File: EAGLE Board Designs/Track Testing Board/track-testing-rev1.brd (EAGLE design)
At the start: 100 x 80 mm, 20 parts, among them J1 CONNECTOR-4_μF_S_RA_, J2 CONNECTOR-4_μF_S_RA_, U1 VOLTAGE_REGULATOR_SOT-23-5_5V, U2 VOLTAGE_REFERENCE_SOIC-8_10V, U3 INA823DT, U4 INA823DT

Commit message: passes drc as is
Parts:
- moved RV1 0.51 mm to (49.8, 45.7)
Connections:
- net STRAIN_GAUGE1_AMPLIFIED: now also A1.D15; no longer A1.D14
- net STRAIN_GAUGE2_AMPLIFIED: now also A1.D14; no longer A1.D15
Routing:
- net STRAIN_GAUGE2_AMPLIFIED: track 46.8 -> 41.5 mm
- net STRAIN_GAUGE1_AMPLIFIED: track 42.9 -> 41.9 mm
- net OUT2-: track 7.01 -> 6.29 mm
- net OUT2+: track 25.8 -> 25.2 mm
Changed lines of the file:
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@@
 <attribute name="NAME" x="35.56" y="77.597" size="0.8128" layer="25" align="bottom-center"/>
 </element>
-<element name="RV1" library="HyTechDevices" package="0603-RES" value="10k" x="49.784" y="45.212" smashed="yes" rot="R180">
-<attribute name="10KOHM" value="https://www.digikey.com/en/products/detail/yageo/RT0603BRD0710KL/1072198" x="49.276" y="45.212" size="1.778" layer="27" rot="R180" display="off"/>
-<attribute name="NAME" x="49.784" y="44.577" size="0.8128" layer="25" font="vector" rot="R180" align="bottom-center"/>
+<element name="RV1" library="HyTechDevices" package="0603-RES" value="10k" x="49.784" y="45.72" smashed="yes" rot="R180">
+<attribute name="10KOHM" value="https://www.digikey.com/en/products/detail/yageo/RT0603BRD0710KL/1072198" x="49.276" y="45.72" size="1.778" layer="27" rot="R180" display="off"/>
+<attribute name="NAME" x="49.784" y="45.085" size="0.8128" layer="25" font="vector" rot="R180" align="bottom-center"/>
 </element>
 <element name="RV5" library="HyTechDevices" package="0603-RES" value="9.88k" x="48.26" y="47.752" smashed="yes">
@@
 <contactref element="U3" pad="4"/>
 <contactref element="J2" pad="2"/>
-<wire x1="30.936" y1="57.952" x2="30.988" y2="57.9" width="0.254" layer="1"/>
 <polygon width="0.254" layer="1">
 <vertex x="-0.508" y="80.772"/>
@@
 <contactref element="C5" pad="2"/>
 <wire x1="56.11" y1="62.2935" x2="56.11" y2="66.9163" width="0" layer="19" extent="1-1"/>
-<wire x1="58.9915" y1="53.467" x2="56.11" y2="62.2935" width="0" layer="19" extent="1-1"/>
+<wire x1="53.7845" y1="53.467" x2="56.11" y2="62.2935" width="0" layer="19" extent="1-1"/>
+<wire x1="58.9915" y1="53.467" x2="53.7845" y2="53.467" width="0" layer="19" extent="1-1"/>
 <wire x1="61.468" y1="54.114" x2="58.9915" y2="53.467" width="0" layer="19" extent="1-1"/>
-<wire x1="53.7845" y1="53.467" x2="58.9915" y2="53.467" width="0" layer="19" extent="1-1"/>
 <wire x1="48.934" y1="55.372" x2="53.7845" y2="53.467" width="0" layer="19" extent="1-1"/>
 <wire x1="43.18" y1="53.606" x2="48.934" y2="55.372" width="0" layer="19" extent="1-1"/>
 <wire x1="35.4965" y1="53.975" x2="43.18" y2="53.606" width="0" layer="19" extent="1-1"/>
 <wire x1="30.988" y1="57.9" x2="35.4965" y2="53.975" width="0" layer="19" extent="1-1"/>
-<wire x1="29.144" y1="57.444" x2="30.936" y2="57.952" width="0" layer="19" extent="1-1"/>
+<wire x1="29.144" y1="57.444" x2="30.988" y2="57.9" width="0" layer="19" extent="1-1"/>
 <wire x1="25.4" y1="55.384" x2="29.144" y2="57.444" width="0" layer="19" extent="1-1"/>
 <wire x1="61.468" y1="44.97" x2="58.9915" y2="53.467" width="0" layer="19" extent="1-1"/>
 <wire x1="58.9915" y1="44.323" x2="61.468" y2="44.97" width="0" layer="19" extent="1-1"/>
 <wire x1="53.7845" y1="44.323" x2="58.9915" y2="44.323" width="0" layer="19" extent="1-1"/>
-<wire x1="48.934" y1="45.212" x2="53.7845" y2="44.323" width="0" layer="19" extent="1-1"/>
+<wire x1="48.934" y1="45.72" x2="53.7845" y2="44.323" width="0" layer="19" extent="1-1"/>
 <wire x1="37.06" y1="66.9163" x2="30.988" y2="57.9" width="0" layer="19" extent="1-1"/>
 <wire x1="20.32" y1="39.37" x2="25.4" y2="55.384" width="0" layer="19" extent="1-1"/>
@@
 <wire x1="53.047" y1="45.593" x2="50.634" y2="43.18" width="0.254" layer="1"/>
 <wire x1="49.11" y1="43.18" x2="50.634" y2="43.18" width="0.254" layer="1"/>
-<wire x1="53.11" y1="62.2935" x2="53.61936875" y2="62.2935" width="0.254" layer="1"/>
 <wire x1="53.11" y1="62.2935" x2="54.356" y2="61.0475" width="0.254" layer="1"/>
 <wire x1="54.356" y1="61.0475" x2="54.356" y2="60.96" width="0.254" layer="1"/>
 <via x="54.356" y="60.96" extent="1-16" drill="0.35"/>
-<wire x1="54.356" y1="60.96" x2="54.864" y2="60.452" width="0.254" layer="16"/>
-<wire x1="54.864" y1="60.452" x2="54.864" y2="48.26" width="0.254" layer="16"/>
-<wire x1="55.88" y1="47.244" x2="55.88" y2="46.228" width="0.254" layer="16"/>
-<wire x1="55.88" y1="47.244" x2="54.864" y2="48.26" width="0.254" layer="16"/>
+<wire x1="54.356" y1="60.96" x2="55.88" y2="59.436" width="0.254" layer="16"/>
+<wire x1="55.88" y1="59.436" x2="55.88" y2="46.228" width="0.254" layer="16"/>
 <via x="55.88" y="46.228" extent="1-16" drill="0.35"/>
 <wire x1="55.88" y1="46.228" x2="55.245" y2="45.593" width="0.254" layer="1"/>
@@
 <contactref element="RV5" pad="2"/>
 <contactref element="U4" pad="2"/>
-<wire x1="50.634" y1="45.212" x2="52.285" y2="46.863" width="0.254" layer="1"/>
-<wire x1="52.285" y1="46.863" x2="53.7845" y2="46.863" width="0.254" layer="1"/>
+<wire x1="50.634" y1="45.72" x2="51.777" y2="46.863" width="0.254" layer="1"/>
+<wire x1="51.777" y1="46.863" x2="53.7845" y2="46.863" width="0.254" layer="1"/>
 <wire x1="49.11" y1="47.752" x2="50.634" y2="46.228" width="0.254" layer="1"/>
-<wire x1="50.634" y1="46.228" x2="50.634" y2="45.212" width="0.254" layer="1"/>
+<wire x1="50.634" y1="46.228" x2="50.634" y2="45.72" width="0.254" layer="1"/>
 </signal>
 <signal name="OUT1-">
@@
 <signal name="STRAIN_GAUGE1_AMPLIFIED">
 <contactref element="U3" pad="6"/>
-<contactref element="A1" pad="D14"/>
-<wire x1="20.32" y1="44.45" x2="26.67" y2="50.8" width="0.254" layer="1"/>
-<wire x1="26.67" y1="50.8" x2="54.356" y2="50.8" width="0.254" layer="1"/>
+<wire x1="47.498" y1="50.8" x2="54.356" y2="50.8" width="0.254" layer="1"/>
 <wire x1="54.356" y1="50.8" x2="58.293" y2="54.737" width="0.254" layer="1"/>
 <wire x1="58.293" y1="54.737" x2="58.9915" y2="54.737" width="0.254" layer="1"/>
+<contactref element="A1" pad="D15"/>
+<wire x1="20.32" y1="46.99" x2="43.688" y2="46.99" width="0.254" layer="1"/>
+<wire x1="43.688" y1="46.99" x2="47.498" y2="50.8" width="0.254" layer="1"/>
 </signal>
 <signal name="STRAIN_GAUGE2_AMPLIFIED">
 <contactref element="U4" pad="6"/>
-<contactref element="A1" pad="D15"/>
-<wire x1="20.32" y1="46.99" x2="18.796" y2="45.466" width="0.254" layer="1"/>
-<wire x1="18.796" y1="43.9932375" x2="19.6092375" y2="43.18" width="0.254" layer="1"/>
-<wire x1="59.1185" y1="45.72" x2="58.9915" y2="45.593" width="0.254" layer="1"/>
-<wire x1="18.796" y1="45.466" x2="18.796" y2="43.9932375" width="0.254" layer="1"/>
-<wire x1="44.704" y1="43.18" x2="46.228" y2="41.656" width="0.254" layer="1"/>
+<wire x1="43.434" y1="44.45" x2="46.228" y2="41.656" width="0.254" layer="1"/>
 <wire x1="46.228" y1="41.656" x2="53.848" y2="41.656" width="0.254" layer="1"/>
-<wire x1="58.8645" y1="45.72" x2="58.9915" y2="45.593" width="0.254" layer="1"/>
-<wire x1="19.6092375" y1="43.18" x2="44.704" y2="43.18" width="0.254" layer="1"/>
+<wire x1="20.32" y1="44.45" x2="43.434" y2="44.45" width="0.254" layer="1"/>
 <wire x1="57.785" y1="45.593" x2="58.9915" y2="45.593" width="0.254" layer="1"/>
 <wire x1="53.848" y1="41.656" x2="57.785" y2="45.593" width="0.254" layer="1"/>
+<contactref element="A1" pad="D14"/>
 </signal>
 <signal name="3.3V">

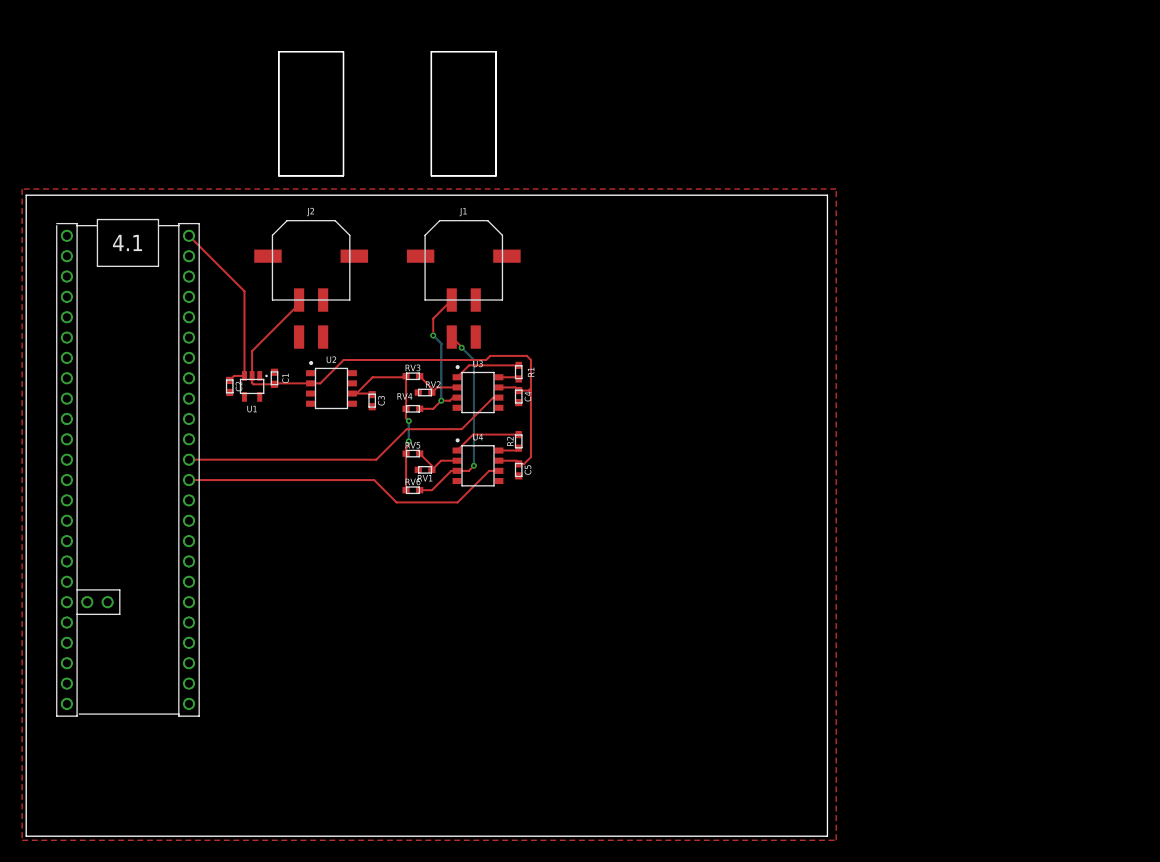
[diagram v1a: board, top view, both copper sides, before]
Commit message: 10 strain gauges and aero uart, passes drc
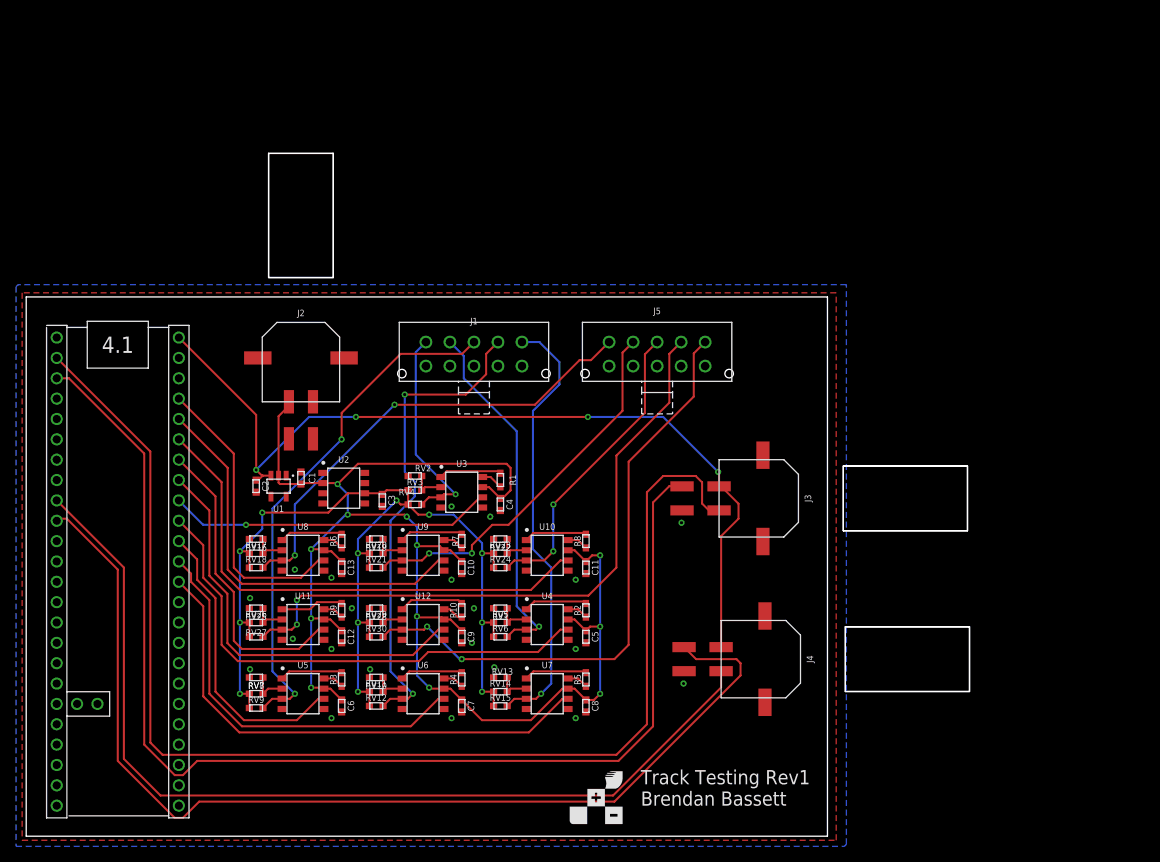
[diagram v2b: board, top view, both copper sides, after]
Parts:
- added C10, C11, C12, C13, C6, C7, C8, C9: CAPACITOR_0603_25V_0.1UF, HyTechDevices:0603-CAP
- added J3, J4: CONNECTOR-4_μF_S_RA_, HyTechDevices:MOLEX_MICROFIT_SMD_RIGHTANGLE_04_DUAL
- added J5: CONNECTOR-10_MF_T_V_, HyTechDevices:MOLEX_MICROFIT_PTH_VERTICAL_10_DUAL
- added R10, R3, R4, R5, R6, R7, R8, R9: RESISTOR_0603_1K, HyTechDevices:0603-RES
- added RV10, RV13, RV16, RV19, RV22, RV25, RV28, RV7: 10k, HyTechDevices:0603-RES
- added RV11, RV14, RV17, RV20, RV23, RV26, RV29, RV8: 9.88k, HyTechDevices:0603-RES
- added RV12, RV15, RV18, RV21, RV24, RV27, RV30, RV9: 118, HyTechDevices:0603-RES
- added U$15: (no value), HyTechManufacturing:LOGO_HYTECH_LARGE
- added U$16: (no value), HyTechManufacturing:LOGO_HYTECH_SQUARE_LARGE
- added U10, U11, U12, U5, U6, U7, U8, U9: INA823DT, HyTechDevices:SOIC-08(NARROW,0.15")
- J1: value CONNECTOR-4_μF_S_RA_ -> CONNECTOR-10_MF_T_V_; device HyTechDevices:MOLEX_MICROFIT_SMD_RIGHTANGLE_04_DUAL -> HyTechDevices:MOLEX_MICROFIT_PTH_VERTICAL_10_DUAL
- moved RV5 23.7 mm to (59.2, 26.7)
- moved R2 22.7 mm to (69.8, 28.2)
- moved C5 22.5 mm to (69.8, 24.9)
- moved U4 21.6 mm to (65.0, 26.4)
- moved RV6 21.3 mm to (59.2, 24.9)
- moved RV1 19.7 mm to (59.2, 28.4)
- moved RV3 14.2 mm to (48.5, 43.2)
- moved J1 13.8 mm to (55.9, 58.7)
- moved C4 13.7 mm to (59.2, 41.4)
- moved R1 13.7 mm to (59.2, 44.5)
- moved C1 12.9 mm to (34.3, 44.7)
- moved C2 12.9 mm to (28.7, 43.7)
- moved U1 12.9 mm to (31.5, 43.7)
- moved A1 12.8 mm to (19.1, 62.2)
- moved J2 12.8 mm to (34.3, 59.7)
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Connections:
- new net N$10: R7.2, U9.1
- new net N$11: R4.1, U6.8
- new net N$12: R5.2, U7.1
- new net N$13: R5.1, U7.8
- new net N$14: R7.1, U9.8
- new net N$15: R8.2, U10.1
- new net N$16: R8.1, U10.8
- new net N$17: R9.2, U11.1
- new net N$18: R9.1, U11.8
- new net N$19: R10.2, U12.1
- new net N$20: R10.1, U12.8
- new net N$5: R3.2, U5.1
- new net N$6: R6.2, U8.1
- new net N$7: R3.1, U5.8
- new net N$8: R6.1, U8.8
- new net N$9: R4.2, U6.1
- new net OUT10+: J5.5, RV30.2, U12.3
- new net OUT10-: RV28.1, RV29.2, U12.2
- new net OUT3+: J1.3, RV9.2, U5.3
- new net OUT3-: RV7.1, RV8.2, U5.2
- new net OUT4+: J1.4, RV12.2, U6.3
- new net OUT4-: RV10.1, RV11.2, U6.2
- new net OUT5+: J1.5, RV15.2, U7.3
- new net OUT5-: RV13.1, RV14.2, U7.2
- new net OUT6+: J5.1, RV18.2, U8.3
- new net OUT6-: RV16.1, RV17.2, U8.2
- new net OUT7+: J5.2, RV21.2, U9.3
- new net OUT7-: RV19.1, RV20.2, U9.2
- new net OUT8+: J5.3, RV24.2, U10.3
- new net OUT8-: RV22.1, RV23.2, U10.2
- new net OUT9+: J5.4, RV27.2, U11.3
- new net OUT9-: RV25.1, RV26.2, U11.2
- new net STRAIN_GAUGE10_AMPLIFIED: A1.D19, U12.6
- new net STRAIN_GAUGE3_AMPLIFIED: A1.D16, U5.6
- new net STRAIN_GAUGE4_AMPLIFIED: A1.D15, U6.6
- new net STRAIN_GAUGE5_AMPLIFIED: A1.D14, U7.6
- new net STRAIN_GAUGE6_AMPLIFIED: A1.D23, U8.6
- new net STRAIN_GAUGE7_AMPLIFIED: A1.D22, U9.6
- new net STRAIN_GAUGE8_AMPLIFIED: A1.D21, U10.6
- new net STRAIN_GAUGE9_AMPLIFIED: A1.D20, U11.6
- new net SURREY_RX1: A1.D1, J3.3
- new net SURREY_RX2: A1.D8, J4.3
- new net SURREY_TX1: A1.D0, J3.2
- new net SURREY_TX2: A1.D7, J4.2
- net +24V: now also C10.1, C11.1, C12.1, C13.1, C6.1, C7.1, C8.1, C9.1, U10.7, U11.7, U12.7, U5.7, U6.7, U7.7, U8.7, U9.7
- net +5V: now also J3.1, J4.1
- net 10V: now also RV11.1, RV12.1, RV14.1, RV15.1, RV17.1, RV18.1, RV20.1, RV21.1, RV23.1, RV24.1, RV26.1, RV27.1, RV29.1, RV30.1, RV8.1, RV9.1
- net GND: now also C10.2, C11.2, C12.2, C13.2, C6.2, C7.2, C8.2, C9.2, J1.10, J1.6, J1.7, J1.8, J1.9, J3.4, J4.4, J5.10, J5.6, J5.7, J5.8, J5.9, RV10.2, RV13.2, RV16.2, RV19.2, RV22.2, RV25.2, RV28.2, RV7.2, U10.4, U10.5, U11.4, U11.5, U12.4, U12.5, U5.4, U5.5, U6.4, U6.5, U7.4, U7.5, U8.4, U8.5, U9.4, U9.5; no longer J1.2, J1.4
- net OUT2+: now also J1.2; no longer J1.3
- net STRAIN_GAUGE1_AMPLIFIED: now also A1.D18; no longer A1.D15
- net STRAIN_GAUGE2_AMPLIFIED: now also A1.D17; no longer A1.D14
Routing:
- net SURREY_TX1: track 0.00 -> 159.2 mm
- net SURREY_RX1: track 0.00 -> 151.2 mm
- net SURREY_RX2: track 0.00 -> 131.7 mm
- net SURREY_TX2: track 0.00 -> 119.8 mm
- net +24V: track 70.0 -> 184.9 mm, vias 0 -> 12
- net 10V: track 24.6 -> 130.7 mm, vias 2 -> 12
- net +5V: track 22.4 -> 110.9 mm, vias 0 -> 4
- net OUT9+: track 0.00 -> 81.0 mm, vias 0 -> 2
- net OUT10+: track 0.00 -> 75.3 mm, vias 0 -> 2
- net STRAIN_GAUGE5_AMPLIFIED: track 0.00 -> 64.7 mm
- net OUT3+: track 0.00 -> 64.7 mm, vias 0 -> 2
- net STRAIN_GAUGE8_AMPLIFIED: track 0.00 -> 64.4 mm
- net OUT4+: track 0.00 -> 60.5 mm, vias 0 -> 2
- net OUT6+: track 0.00 -> 58.6 mm, vias 0 -> 2
- net OUT5+: track 0.00 -> 54.8 mm, vias 0 -> 1
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- added copper zone on layer 16, net GND
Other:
- board size 100 x 80 mm -> 100 x 67.3 mm
- board text added: "Track Testing Rev1 Brendan Bassett"

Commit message: track testing board
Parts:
- removed U$15: (no value), HyTechManufacturing:LOGO_HYTECH_LARGE
- removed U$16: (no value), HyTechManufacturing:LOGO_HYTECH_SQUARE_LARGE
- added C14, C17, C18, C54, C55: CAPACITOR_0603_10V_0.1UF, HyTechDevices:0603-CAP
- added C15, C16, C56, C57: CAPACITOR_0603_10V_1UF, HyTechDevices:0603-CAP
- added C19, C20: CAPACITOR_0603_25V_10UF, HyTechDevices:0603-CAP
- added J6: CONNECTOR-4_μF_S_RA_, HyTechDevices:MOLEX_MICROFIT_SMD_RIGHTANGLE_04_DUAL
- added R11, R12, R13, R14, R15, R16, R18, R20, R27, R29: RESISTOR_0603_41.2K, HyTechDevices:0603-RES
- added R17, R19, R21, R22, R23, R24, R25, R26, R28, R30: RESISTOR_0603_1K, HyTechDevices:0603-RES
- added U13, U14, U15, U16, U17, U18, U19, U20, U21, U23: OPAMP_1_CHANNEL_OPA991, HyTechDevices:SC-70-5
- added U22: ADC128S022, HyTechDevices:TSSOP-16
- added U24: TCAN1051HQV-Q1, HyTechDevices:SOIC-08(NARROW,0.15")
- added U25: VOLTAGE_REGULATOR_SOT-223_3.3V, HyTechDevices:SOT-223
- added VR1, VR10, VR2, VR3, VR4, VR5, VR6, VR7, VR8, VR9: RESISTOR_TRIMPOT_10K_3362P, HyTechDevices:3362P
- C3: value CAPACITOR_0603_25V_1UF -> CAPACITOR_0603_10V_0.1UF
- R1, R10, R2, R3, R4, R5, R6, R7, R8, R9: value RESISTOR_0603_1K -> RESISTOR_0603_402
- RV1, RV10, RV13, RV16, RV19, RV2, RV22, RV25, RV28, RV7: value 10k -> 1M
- RV11, RV14, RV17, RV20, RV23, RV26, RV29, RV3, RV5, RV8: value 9.88k -> 1M
- RV12, RV15, RV18, RV21, RV24, RV27, RV30, RV4, RV6, RV9: value 118 -> 120
- U2: value VOLTAGE_REFERENCE_SOIC-8_10V -> ADC128S022; device HyTechDevices:SOIC-08(NARROW,0.15") -> HyTechDevices:TSSOP-16
- moved R6 56.0 mm to (91.4, 57.5), turned to 270 degrees
- moved U8 55.2 mm to (85.6, 56.1)
- moved C13 53.8 mm to (91.6, 20.3)
- moved C12 52.1 mm to (91.3, 29.3)
- moved R9 52.1 mm to (91.3, 32.6), turned to 270 degrees
- moved U11 51.2 mm to (85.6, 30.7)
- moved A1 48.0 mm to (4.83, 16.4), turned to 0 degrees
- moved C9 47.1 mm to (91.4, 54.0)
- moved RV16 46.9 mm to (70.2, 58.8)
- moved RV17 46.3 mm to (70.2, 55.9)
- moved RV18 45.8 mm to (70.2, 52.8)
- moved RV25 41.8 mm to (70.2, 33.3)
- moved RV26 41.7 mm to (70.2, 30.7)
- moved RV27 41.7 mm to (70.2, 28.2)
- moved C10 39.4 mm to (91.4, 46.7)
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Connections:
- removed net 10V: C3.1, RV11.1, RV12.1, RV14.1, RV15.1, RV17.1, RV18.1, RV20.1, RV21.1, RV23.1, RV24.1, RV26.1, RV27.1, RV29.1, RV3.1, RV30.1, RV4.1, RV5.1, RV6.1, RV8.1, RV9.1, U2.6
- new net !AD1_CS: A1.D33, U2.1
- new net !AD2_CS: A1.D34, U22.1
- new net +3V3: C15.1, C18.1, C20.1, C3.1, C54.1, C56.1, U2.13, U22.13, U24.5, U25.2, U25.4
- new net CANH: J6.3, U24.7
- new net CANL: J6.4, U24.6
- new net CAN_TT_RX: A1.D23, U24.4
- new net CAN_TT_TX: A1.D22, U24.1
- new net N$21: R12.2, R22.1, U13.3
- new net N$22: R11.2, R21.1, U23.3
- new net N$23: R13.2, R23.1, U14.3
- new net N$24: R14.2, R24.1, U15.3
- new net N$25: R15.2, R25.1, U16.3
- new net N$26: R16.2, R17.1, U17.3
- new net N$27: R18.2, R19.1, U18.3
- new net N$28: R20.2, R26.1, U19.3
- new net N$29: R27.2, R28.1, U20.3
- new net N$30: R29.2, R30.1, U21.3
- new net N$41: RV2.1, VR1.1
- new net N$42: RV3.2, VR1.3
- new net N$44: RV1.1, VR2.1
- new net N$45: RV5.2, VR2.3
- new net N$46: RV11.2, VR4.3
- new net N$47: RV7.1, VR3.1
- new net N$48: RV8.2, VR3.3
- new net N$49: RV10.1, VR4.1
- new net N$50: RV14.2, VR5.3
- new net N$51: RV13.1, VR5.1
- new net N$52: RV16.1, VR6.1
- new net N$53: RV17.2, VR6.3
- new net N$54: RV19.1, VR7.1
- new net N$55: RV20.2, VR7.3
- new net N$56: RV22.1, VR8.1
- new net N$57: RV23.2, VR8.3
- new net N$58: RV25.1, VR9.1
- new net N$59: RV26.2, VR9.3
- new net N$60: RV28.1, VR10.1
- new net N$61: RV29.2, VR10.3
- new net STRAIN_GAUGE10_INTER: U12.6, U21.1
- new net STRAIN_GAUGE1_INTER: U23.1, U3.6
- new net STRAIN_GAUGE2_INTER: U13.1, U4.6
- new net STRAIN_GAUGE3_INTER: U14.1, U5.6
- new net STRAIN_GAUGE4_INTER: U15.1, U6.6
- new net STRAIN_GAUGE5_INTER: U16.1, U7.6
- new net STRAIN_GAUGE6_INTER: U17.1, U8.6
- new net STRAIN_GAUGE7_INTER: U18.1, U9.6
- new net STRAIN_GAUGE8_INTER: U10.6, U19.1
- new net STRAIN_GAUGE9_INTER: U11.6, U20.1
- new net TT_CLK: A1.D13, U2.16, U22.16
- new net TT_SDI: A1.D12, U2.15, U22.15
- new net TT_SDO: A1.D11, U2.14, U22.14
- net +24V: no longer C10.1, C11.1, C12.1, C13.1, C4.1, C5.1, C6.1, C7.1, C8.1, C9.1, U10.7, U11.7, U12.7, U2.2, U3.7, U4.7, U5.7, U6.7, U7.7, U8.7, U9.7
- net +5V: now also C10.1, C11.1, C12.1, C13.1, C14.1, C16.1, C17.1, C19.1, C4.1, C5.1, C55.1, C57.1, C6.1, C7.1, C8.1, C9.1, J6.1, RV11.1, RV12.1, RV14.1, RV15.1, RV17.1, RV18.1, RV20.1, RV21.1, RV23.1, RV24.1, RV26.1, RV27.1, RV29.1, RV3.1, RV30.1, RV4.1, RV5.1, RV6.1, RV8.1, RV9.1, U10.7, U11.7, U12.7, U13.5, U14.5, U15.5, U16.5, U17.5, U18.5, U19.5, U2.2, U20.5, U21.5, U22.2, U23.5, U24.3, U25.3, U3.7, U4.7, U5.7, U6.7, U7.7, U8.7, U9.7
- net GND: now also C14.2, C15.2, C16.2, C17.2, C18.2, C19.2, C20.2, C54.2, C55.2, C56.2, C57.2, J6.2, R17.2, R19.2, R21.2, R22.2, R23.2, R24.2, R25.2, R26.2, R28.2, R30.2, U13.2, U14.2, U15.2, U16.2, U17.2, U18.2, U19.2, U2.12, U2.3, U20.2, U21.2, U22.12, U22.3, U23.2, U24.2, U24.8, U25.1; no longer U2.4
- net OUT1+: now also J5.5; no longer J1.1
- net OUT1-: now also VR1.2; no longer RV2.1, RV3.2
- net OUT10+: now also J1.2; no longer J5.5
- net OUT10-: now also VR10.2; no longer RV28.1, RV29.2
- net OUT2+: now also J5.4; no longer J1.2
- net OUT2-: now also VR2.2; no longer RV1.1, RV5.2
- net OUT3+: now also J1.5; no longer J1.3
- net OUT3-: now also VR3.2; no longer RV7.1, RV8.2
- net OUT4-: now also VR4.2; no longer RV10.1, RV11.2
- net OUT5+: now also J1.3; no longer J1.5
- net OUT5-: now also VR5.2; no longer RV13.1, RV14.2
- net OUT6-: now also VR6.2; no longer RV16.1, RV17.2
- net OUT7-: now also VR7.2; no longer RV19.1, RV20.2
- net OUT8-: now also VR8.2; no longer RV22.1, RV23.2
- net OUT9+: now also J1.1; no longer J5.4
- net OUT9-: now also VR9.2; no longer RV25.1, RV26.2
- net STRAIN_GAUGE10_AMPLIFIED: now also R29.1, U21.4, U22.5; no longer A1.D19, U12.6
- net STRAIN_GAUGE1_AMPLIFIED: now also R11.1, U2.4, U23.4; no longer A1.D18, U3.6
- net STRAIN_GAUGE2_AMPLIFIED: now also R12.1, U13.4, U2.5; no longer A1.D17, U4.6
- net STRAIN_GAUGE3_AMPLIFIED: now also R13.1, U14.4, U2.6; no longer A1.D16, U5.6
- net STRAIN_GAUGE4_AMPLIFIED: now also R14.1, U15.4, U22.10; no longer A1.D15, U6.6
- net STRAIN_GAUGE5_AMPLIFIED: now also R15.1, U16.4, U22.11; no longer A1.D14, U7.6
- net STRAIN_GAUGE6_AMPLIFIED: now also R16.1, U17.4, U2.9; no longer A1.D23, U8.6
- net STRAIN_GAUGE7_AMPLIFIED: now also R18.1, U18.4, U2.10; no longer A1.D22, U9.6
- net STRAIN_GAUGE8_AMPLIFIED: now also R20.1, U19.4, U2.11; no longer A1.D21, U10.6
- net STRAIN_GAUGE9_AMPLIFIED: now also R27.1, U20.4, U22.4; no longer A1.D20, U11.6
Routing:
- net +5V: track 110.9 -> 588.8 mm, vias 4 -> 0
- net CAN_TT_RX: track 0.00 -> 171.6 mm, vias 0 -> 7
- net CAN_TT_TX: track 0.00 -> 162.6 mm, vias 0 -> 5
- net +24V: track 184.9 -> 26.9 mm, vias 12 -> 0
- net 10V: track 130.7 -> 0.00 mm, vias 12 -> 0
- net +3V3: track 0.00 -> 114.4 mm, vias 0 -> 4
- net OUT5+: track 54.8 -> 150.5 mm
- net OUT4+: track 60.5 -> 143.4 mm, vias 2 -> 6
- net !AD2_CS: track 0.00 -> 76.4 mm, vias 0 -> 2
- net TT_CLK: track 0.00 -> 67.9 mm, vias 0 -> 2
- net STRAIN_GAUGE6_AMPLIFIED: track 36.6 -> 99.3 mm, vias 0 -> 2
- net STRAIN_GAUGE9_AMPLIFIED: track 38.1 -> 98.1 mm, vias 0 -> 4
- net STRAIN_GAUGE8_AMPLIFIED: track 64.4 -> 117.9 mm, vias 0 -> 4
- net STRAIN_GAUGE7_AMPLIFIED: track 50.3 -> 103.2 mm, vias 0 -> 2
- net !AD1_CS: track 0.00 -> 48.9 mm, vias 0 -> 1
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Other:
- board size 100 x 67.3 mm -> 121.9 x 84.8 mm
- board text removed: "Track Testing Rev1 Brendan Bassett"
